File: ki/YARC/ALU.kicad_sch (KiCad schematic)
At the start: 7 parts, among them U116 AS6C6264, U117 AS6C6264, U118 AS6C6264, U119 74LS245, U120 74LS245, U121 74LS573, U122 74LS574

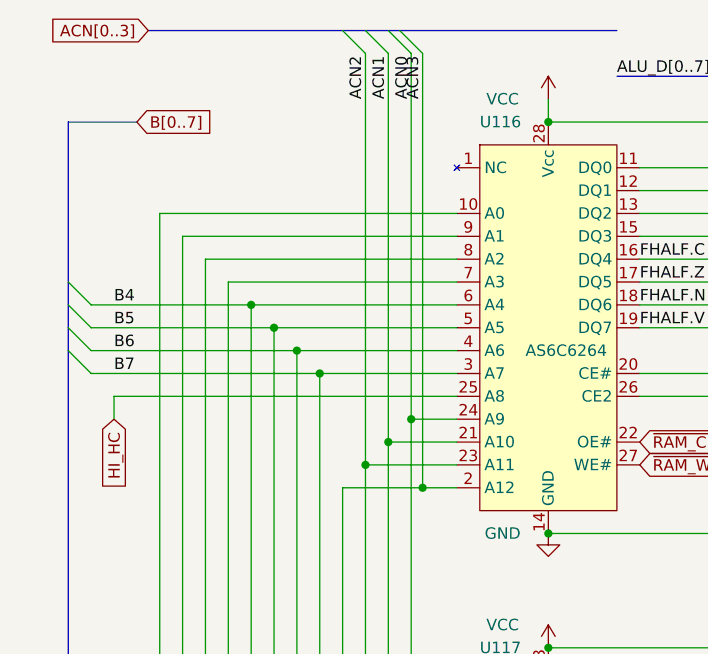
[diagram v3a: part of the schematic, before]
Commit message: Make main schematic match V503 schematic control signal naming and minor layout cleanup
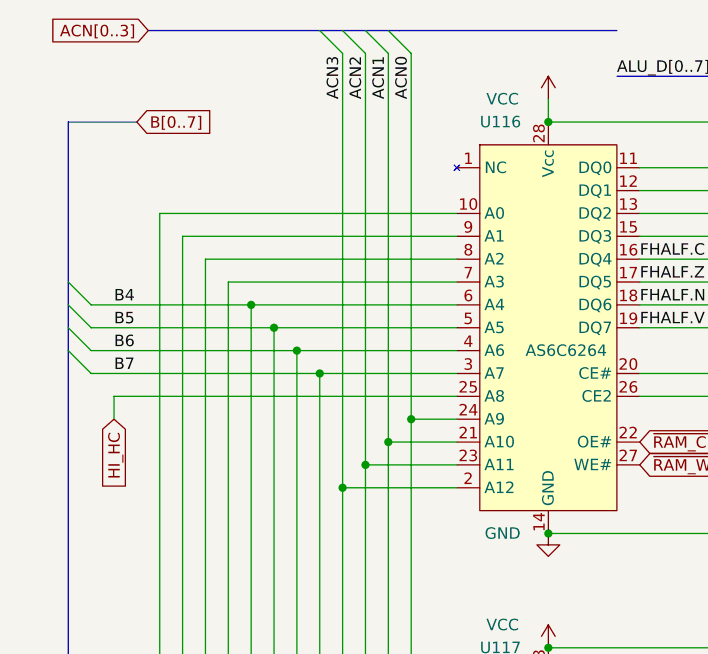
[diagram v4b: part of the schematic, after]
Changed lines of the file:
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@@
   (junction (at 114.3 116.84) (diameter 0) (color 0 0 0 0)
   )
+  (junction (at 45.72 66.04) (diameter 0) (color 0 0 0 0)
+  )
   (junction (at 43.18 53.34) (diameter 0) (color 0 0 0 0)
   )
@@
   (junction (at 35.56 45.72) (diameter 0) (color 0 0 0 0)
   )
-  (junction (at 54.61 66.04) (diameter 0) (color 0 0 0 0)
-  )
   (junction (at 50.8 119.38) (diameter 0) (color 0 0 0 0)
   )
@@
     (stroke (width 0) (type default))
   )
-  (bus_entry (at 52.07 15.24) (size 2.54 2.54)
-    (stroke (width 0) (type default))
-  )
   (bus_entry (at 264.16 38.1) (size -2.54 2.54)
     (stroke (width 0) (type default))
@@
     (stroke (width 0) (type default))
   )
+  (bus_entry (at 43.18 15.24) (size 2.54 2.54)
+    (stroke (width 0) (type default))
+  )
   (bus_entry (at 264.16 25.4) (size -2.54 2.54)
     (stroke (width 0) (type default))
@@
     (stroke (width 0) (type default))
   )
-  (wire (pts (xy 58.42 66.04) (xy 54.61 66.04))
+  (wire (pts (xy 45.72 66.04) (xy 58.42 66.04))
     (stroke (width 0) (type default))
   )
@@
     (stroke (width 0) (type default))
   )
-  (wire (pts (xy 54.61 66.04) (xy 45.72 66.04))
-    (stroke (width 0) (type default))
-  )
   (wire (pts (xy 101.6 60.96) (xy 160.02 60.96))
     (stroke (width 0) (type default))
@@
     (stroke (width 0) (type default))
   )
+  (bus (pts (xy 43.18 15.24) (xy 45.72 15.24))
+    (stroke (width 0) (type default))
+  )
   (bus (pts (xy 257.81 15.24) (xy 264.16 15.24))
     (stroke (width 0) (type default))
@@
     (stroke (width 0) (type default))
   )
-  (wire (pts (xy 54.61 17.78) (xy 54.61 66.04))
-    (stroke (width 0) (type default))
-  )
   (wire (pts (xy 91.44 25.4) (xy 68.58 25.4))
     (stroke (width 0) (type default))
@@
     (stroke (width 0) (type default))
   )
-  (bus (pts (xy 24.13 15.24) (xy 45.72 15.24))
+  (bus (pts (xy 24.13 15.24) (xy 43.18 15.24))
     (stroke (width 0) (type default))
   )
@@
     (stroke (width 0) (type default))
   )
+  (wire (pts (xy 45.72 17.78) (xy 45.72 66.04))
+    (stroke (width 0) (type default))
+  )
   (bus (pts (xy 50.8 15.24) (xy 52.07 15.24))
     (stroke (width 0) (type default))
@@
   )
   (label "FHALF.Z" (at 127 68.58 0) (fields_autoplaced)
-    (effects (font (size 1.27 1.27)) (justify left bottom))
-  )
-  (label "ACN3" (at 54.61 22.86 90) (fields_autoplaced)
     (effects (font (size 1.27 1.27)) (justify left bottom))
   )
@@
     (effects (font (size 1.27 1.27)) (justify left bottom))
   )
+  (label "ACN3" (at 45.72 22.86 90)
+    (effects (font (size 1.27 1.27)) (justify left bottom))
+  )

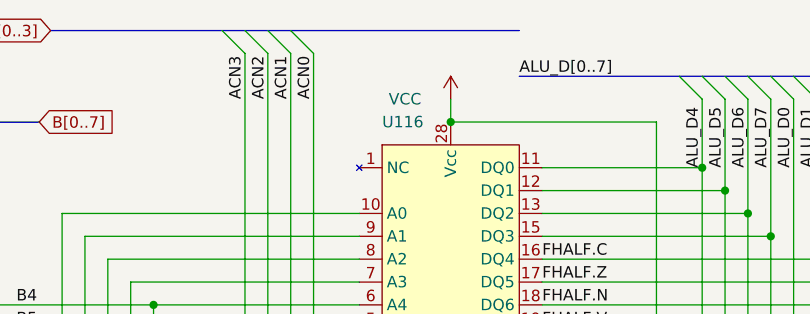
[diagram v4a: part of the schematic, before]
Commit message: Disable sysaddr_src decoder when the Nano has control of the address bus (the Nano never disables its address transceivers when it has control)
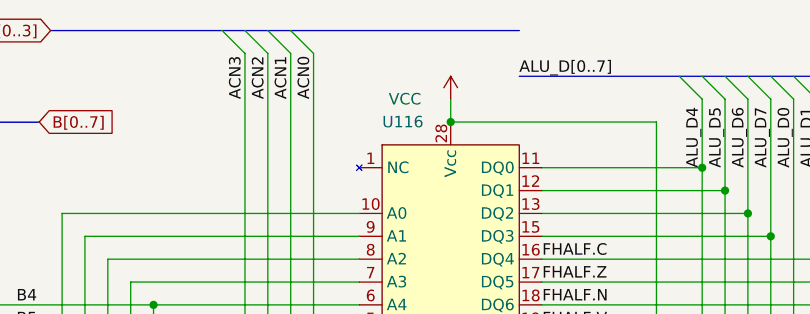
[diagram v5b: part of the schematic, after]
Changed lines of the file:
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@@
     (stroke (width 0) (type default))
   )
-  (bus (pts (xy 50.8 15.24) (xy 52.07 15.24))
+  (bus (pts (xy 50.8 15.24) (xy 76.2 15.24))
     (stroke (width 0) (type default))
   )
@@
   )
   (wire (pts (xy 190.5 55.88) (xy 185.42 55.88))
-    (stroke (width 0) (type default))
-  )
-  (bus (pts (xy 52.07 15.24) (xy 76.2 15.24))
     (stroke (width 0) (type default))
   )
@@
     (effects (font (size 1.27 1.27)) (justify left bottom))
   )
-  (label "ACN3" (at 45.72 22.86 90)
-    (effects (font (size 1.27 1.27)) (justify left bottom))
-  )
+  (label "ACN3" (at 45.72 22.86 90) (fields_autoplaced)
+    (effects (font (size 1.27 1.27)) (justify left bottom))
+  )
